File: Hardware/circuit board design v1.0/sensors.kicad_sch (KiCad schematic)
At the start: 8 parts, among them IC1 BMI088, U4 BME280

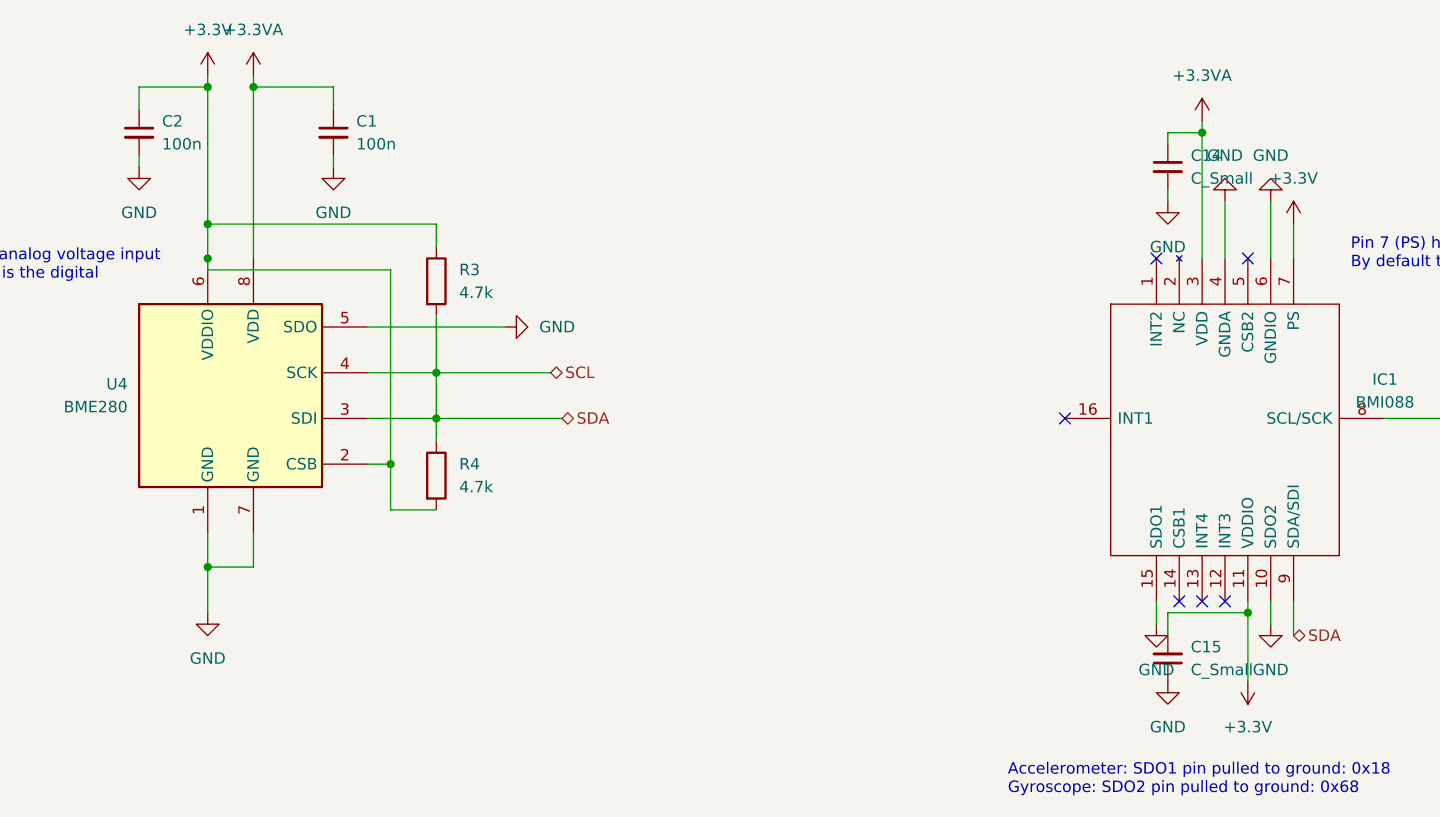
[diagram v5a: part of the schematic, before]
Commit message: Placed components but not connected yet
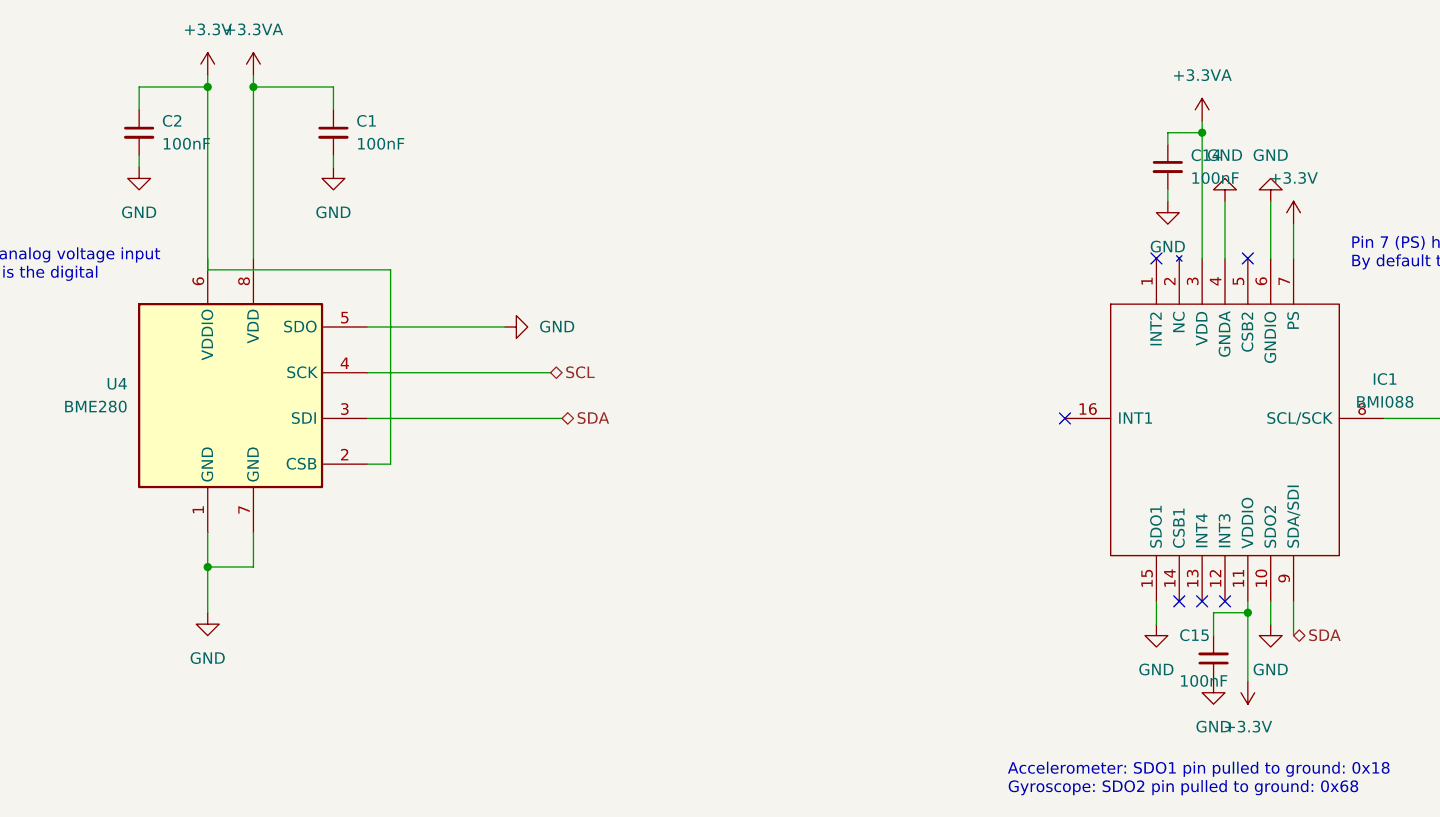
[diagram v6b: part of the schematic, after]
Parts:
- removed R3, R4: 4.7k, Resistor_SMD:R_0603_1608Metric, symbol Device:R
- C1, C2: value 100n -> 100nF
- C14, C15: value C_Small -> 100nF
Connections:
- net +3.3V: no longer U4.6 (VDDIO)
- net SCL: no longer IC1.9 (SDA/SDI), U4.3 (SDI)
- new net SDA: IC1.9 (SDA/SDI), U4.3 (SDI)
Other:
- moved on the sheet: C15
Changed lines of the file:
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@@
   (junction (at 166.37 35.56) (diameter 0) (color 0 0 0 0)
   )
-  (junction (at 81.28 62.23) (diameter 0) (color 0 0 0 0)
-  )
-  (junction (at 81.28 67.31) (diameter 0) (color 0 0 0 0)
-  )
   (junction (at 55.88 83.82) (diameter 0) (color 0 0 0 0)
   )
@@
   )
   (junction (at 60.96 30.48) (diameter 0) (color 0 0 0 0)
-  )
-  (junction (at 76.2 72.39) (diameter 0) (color 0 0 0 0)
-  )
-  (junction (at 55.88 45.72) (diameter 0) (color 0 0 0 0)
-  )
-  (junction (at 55.88 49.53) (diameter 0) (color 0 0 0 0)
   )
   (no_connect (at 166.37 87.63))
@@
     (stroke (width 0) (type default) (color 0 0 0 0))
   )
-  (wire (pts (xy 81.28 62.23) (xy 81.28 55.88))
-    (stroke (width 0) (type default) (color 0 0 0 0))
-  )
-  (wire (pts (xy 81.28 67.31) (xy 95.25 67.31))
-    (stroke (width 0) (type default) (color 0 0 0 0))
-  )
-  (wire (pts (xy 81.28 77.47) (xy 76.2 77.47))
-    (stroke (width 0) (type default) (color 0 0 0 0))
-  )
   (wire (pts (xy 73.66 72.39) (xy 76.2 72.39))
     (stroke (width 0) (type default) (color 0 0 0 0))
   )
-  (wire (pts (xy 81.28 62.23) (xy 81.28 67.31))
-    (stroke (width 0) (type default) (color 0 0 0 0))
-  )
   (wire (pts (xy 60.96 80.01) (xy 60.96 83.82))
     (stroke (width 0) (type default) (color 0 0 0 0))
@@
     (stroke (width 0) (type default) (color 0 0 0 0))
   )
-  (wire (pts (xy 55.88 50.8) (xy 55.88 49.53))
-    (stroke (width 0) (type default) (color 0 0 0 0))
-  )
-  (wire (pts (xy 162.56 88.9) (xy 171.45 88.9))
-    (stroke (width 0) (type default) (color 0 0 0 0))
-  )
-  (wire (pts (xy 76.2 72.39) (xy 76.2 77.47))
-    (stroke (width 0) (type default) (color 0 0 0 0))
-  )
-  (wire (pts (xy 73.66 62.23) (xy 81.28 62.23))
+  (wire (pts (xy 55.88 30.48) (xy 55.88 50.8))
     (stroke (width 0) (type default) (color 0 0 0 0))
   )
@@
     (stroke (width 0) (type default) (color 0 0 0 0))
   )
-  (wire (pts (xy 73.66 67.31) (xy 81.28 67.31))
-    (stroke (width 0) (type default) (color 0 0 0 0))
-  )
-  (wire (pts (xy 81.28 67.31) (xy 81.28 69.85))
-    (stroke (width 0) (type default) (color 0 0 0 0))
-  )
-  (wire (pts (xy 81.28 62.23) (xy 93.98 62.23))
-    (stroke (width 0) (type default) (color 0 0 0 0))
-  )
-  (wire (pts (xy 81.28 48.26) (xy 81.28 45.72))
+  (wire (pts (xy 73.66 67.31) (xy 95.25 67.31))
+    (stroke (width 0) (type default) (color 0 0 0 0))
+  )
+  (wire (pts (xy 73.66 62.23) (xy 93.98 62.23))
     (stroke (width 0) (type default) (color 0 0 0 0))
   )
@@
     (stroke (width 0) (type default) (color 0 0 0 0))
   )
-  (wire (pts (xy 55.88 30.48) (xy 55.88 45.72))
-    (stroke (width 0) (type default) (color 0 0 0 0))
-  )
   (wire (pts (xy 69.85 33.02) (xy 69.85 30.48))
     (stroke (width 0) (type default) (color 0 0 0 0))
   )
-  (wire (pts (xy 162.56 91.44) (xy 162.56 88.9))
-    (stroke (width 0) (type default) (color 0 0 0 0))
-  )
-  (wire (pts (xy 81.28 45.72) (xy 55.88 45.72))
-    (stroke (width 0) (type default) (color 0 0 0 0))
-  )
   (wire (pts (xy 161.29 87.63) (xy 161.29 90.17))
     (stroke (width 0) (type default) (color 0 0 0 0))
   )
+  (wire (pts (xy 167.64 88.9) (xy 171.45 88.9))
+    (stroke (width 0) (type default) (color 0 0 0 0))
+  )
   (wire (pts (xy 166.37 34.29) (xy 166.37 35.56))
     (stroke (width 0) (type default) (color 0 0 0 0))
@@
     (stroke (width 0) (type default) (color 0 0 0 0))
   )
-  (wire (pts (xy 55.88 45.72) (xy 55.88 49.53))
-    (stroke (width 0) (type default) (color 0 0 0 0))
-  )
   (wire (pts (xy 60.96 30.48) (xy 60.96 49.53))
     (stroke (width 0) (type default) (color 0 0 0 0))
@@
   )
   (wire (pts (xy 186.69 67.31) (xy 193.04 67.31))
+    (stroke (width 0) (type default) (color 0 0 0 0))
+  )
+  (wire (pts (xy 167.64 88.9) (xy 167.64 91.44))
     (stroke (width 0) (type default) (color 0 0 0 0))
   )
@@
       (effects (font (size 1.27 1.27)) (justify left))
     )
-    (property "Value" "100n" (id 1) (at 50.8 36.8362 0)
+    (property "Value" "100nF" (id 1) (at 50.8 36.8362 0)
       (effects (font (size 1.27 1.27)) (justify left))
     )
@@
       (effects (font (size 1.27 1.27)) (justify left))
     )
-    (property "Value" "C_Small" (id 1) (at 165.1 40.6462 0)
+    (property "Value" "100nF" (id 1) (at 165.1 40.6462 0)
       (effects (font (size 1.27 1.27)) (justify left))
     )
@@
     (pin "2")
   )
-  (symbol (lib_id "power:GND") (at 162.56 96.52 0) (unit 1)
-    (in_bom yes) (on_board yes) (fields_autoplaced)
-    (property "Reference" "#PWR0136" (id 0) (at 162.56 102.87 0)
-      (effects (font (size 1.27 1.27)) hide)
-    )
-    (property "Value" "GND" (id 1) (at 162.56 101.6 0))
-    (property "Footprint" "" (id 2) (at 162.56 96.52 0)
-      (effects (font (size 1.27 1.27)) hide)
-    )
-    (property "Datasheet" "" (id 3) (at 162.56 96.52 0)
+  (symbol (lib_id "power:GND") (at 167.64 96.52 0) (unit 1)
+    (in_bom yes) (on_board yes) (fields_autoplaced)
+    (property "Reference" "#PWR0136" (id 0) (at 167.64 102.87 0)
+      (effects (font (size 1.27 1.27)) hide)
+    )
+    (property "Value" "GND" (id 1) (at 167.64 101.6 0))
+    (property "Footprint" "" (id 2) (at 167.64 96.52 0)
+      (effects (font (size 1.27 1.27)) hide)
+    )
+    (property "Datasheet" "" (id 3) (at 167.64 96.52 0)
       (effects (font (size 1.27 1.27)) hide)
     )
@@
     (pin "1")
   )
-  (symbol (lib_id "Device:R") (at 81.28 73.66 0) (unit 1)
-    (in_bom yes) (on_board yes) (fields_autoplaced)
-    (property "Reference" "R4" (id 0) (at 83.82 72.3899 0)
-      (effects (font (size 1.27 1.27)) (justify left))
-    )
-    (property "Value" "4.7k" (id 1) (at 83.82 74.9299 0)
-      (effects (font (size 1.27 1.27)) (justify left))
-    )
-    (property "Footprint" "Resistor_SMD:R_0603_1608Metric" (id 2) (at 79.502 73.66 90)
-      (effects (font (size 1.27 1.27)) hide)
-    )
-    (property "Datasheet" "~" (id 3) (at 81.28 73.66 0)
-      (effects (font (size 1.27 1.27)) hide)
-    )
-    (pin "1")
-    (pin "2")
-  )
   (symbol (lib_id "Device:C_Small") (at 69.85 35.56 0) (unit 1)
     (in_bom yes) (on_board yes) (fields_autoplaced)
@@
       (effects (font (size 1.27 1.27)) (justify left))
     )
-    (property "Value" "100n" (id 1) (at 72.39 36.8362 0)
+    (property "Value" "100nF" (id 1) (at 72.39 36.8362 0)
       (effects (font (size 1.27 1.27)) (justify left))
     )
@@
     (pin "8")
   )
-  (symbol (lib_id "Device:C_Small") (at 162.56 93.98 180) (unit 1)
-    (in_bom yes) (on_board yes) (fields_autoplaced)
-    (property "Reference" "C15" (id 0) (at 165.1 92.7035 0)
+  (symbol (lib_id "Device:C_Small") (at 167.64 93.98 180) (unit 1)
+    (in_bom yes) (on_board yes)
+    (property "Reference" "C15" (id 0) (at 163.83 91.44 0)
       (effects (font (size 1.27 1.27)) (justify right))
     )
-    (property "Value" "C_Small" (id 1) (at 165.1 95.2435 0)
+    (property "Value" "100nF" (id 1) (at 163.83 96.52 0)
       (effects (font (size 1.27 1.27)) (justify right))
     )
-    (property "Footprint" "Capacitor_SMD:C_0603_1608Metric" (id 2) (at 162.56 93.98 0)
-      (effects (font (size 1.27 1.27)) hide)
-    )
-    (property "Datasheet" "~" (id 3) (at 162.56 93.98 0)
-      (effects (font (size 1.27 1.27)) hide)
-    )
-    (pin "1")
-    (pin "2")
-  )
-  (symbol (lib_id "Device:R") (at 81.28 52.07 0) (unit 1)
-    (in_bom yes) (on_board yes) (fields_autoplaced)
-    (property "Reference" "R3" (id 0) (at 83.82 50.7999 0)
-      (effects (font (size 1.27 1.27)) (justify left))
-    )
-    (property "Value" "4.7k" (id 1) (at 83.82 53.3399 0)
-      (effects (font (size 1.27 1.27)) (justify left))
-    )
-    (property "Footprint" "Resistor_SMD:R_0603_1608Metric" (id 2) (at 79.502 52.07 90)
-      (effects (font (size 1.27 1.27)) hide)
-    )
-    (property "Datasheet" "~" (id 3) (at 81.28 52.07 0)
-      (effects (font (size 1.27 1.27)) hide)
-    )
+    (property "Footprint" "Capacitor_SMD:C_0603_1608Metric" (id 2) (at 167.64 93.98 0)
+      (effects (font (size 1.27 1.27)) hide)
+    )
+    (property "Datasheet" "~" (id 3) (at 167.64 93.98 0)
+      (effects (font (size 1.27 1.27)) hide)
+    )

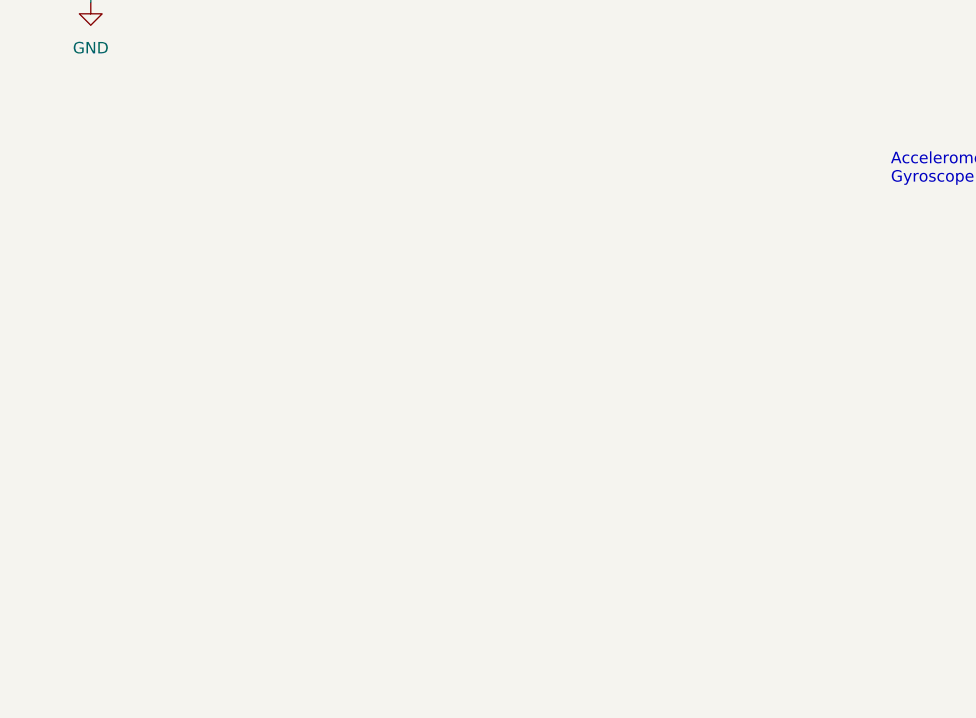
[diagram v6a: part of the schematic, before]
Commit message: Added radio connections to pcb and code
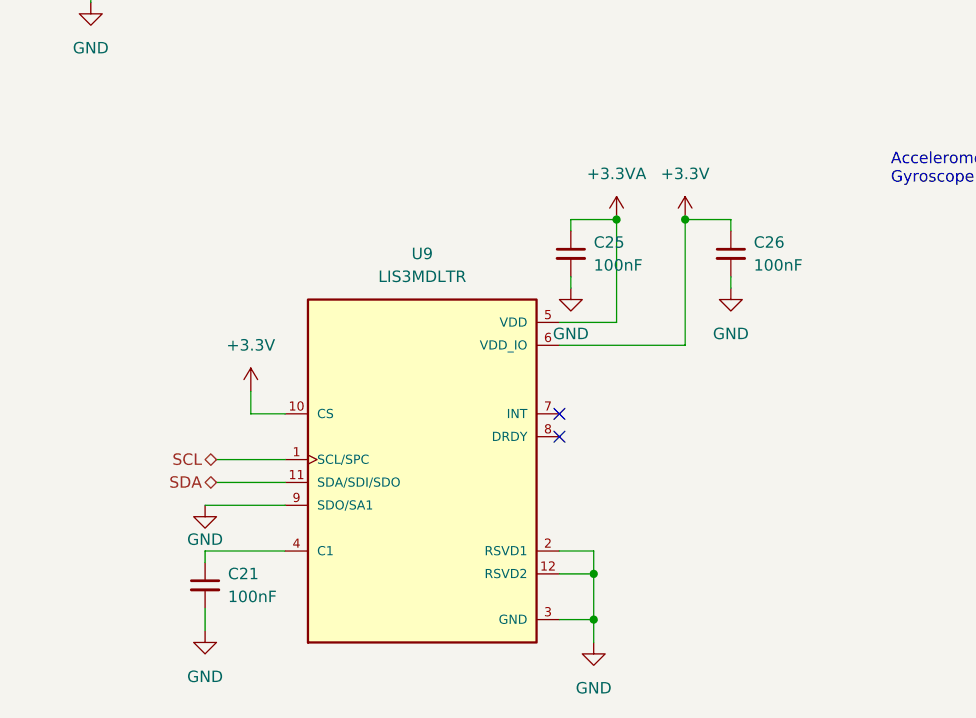
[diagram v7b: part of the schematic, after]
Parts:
- added C21, C25, C26: 100nF, Capacitor_SMD:C_0603_1608Metric, symbol Device:C_Small
- added U9: LIS3MDLTR, Components:XDCR_LIS3MDLTR, symbol Components:LIS3MDLTR
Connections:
- net +3.3V: now also C26.1, U9.10 (CS), U9.6 (VDD_IO)
- net +3.3VA: now also C25.1, U9.5 (VDD)
- net GND: now also C21.2, C25.2, C26.2, U9.12 (RSVD2), U9.2 (RSVD1), U9.3 (GND), U9.9 (SDO/SA1)
- net SCL: now also U9.1 (SCL/SPC)
- net SDA: now also U9.11 (SDA/SDI/SDO)
- new net: C21.1, U9.4 (C1)
- no-connect marks 6 -> 8
